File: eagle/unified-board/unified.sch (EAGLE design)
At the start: 286 parts, among them IC101 THAT151x, IC201 THAT151x, IC301 THAT151x, IC401 THAT151x, J103 phantom, J104 eqout, J105 eqout, J203 phantom, J204 eqout, J205 eqout, J303 phantom, J304 eqout, J305 eqout, J403 phantom, J404 eqout, J405 eqout, J501 out2, J601 out2, J701 power, U101 lme49710, U201 lme49710, U301 lme49710, U401 lme49710, U501 lme49710, U502 LM3915N, U601 lme49710, U602 LM3915N

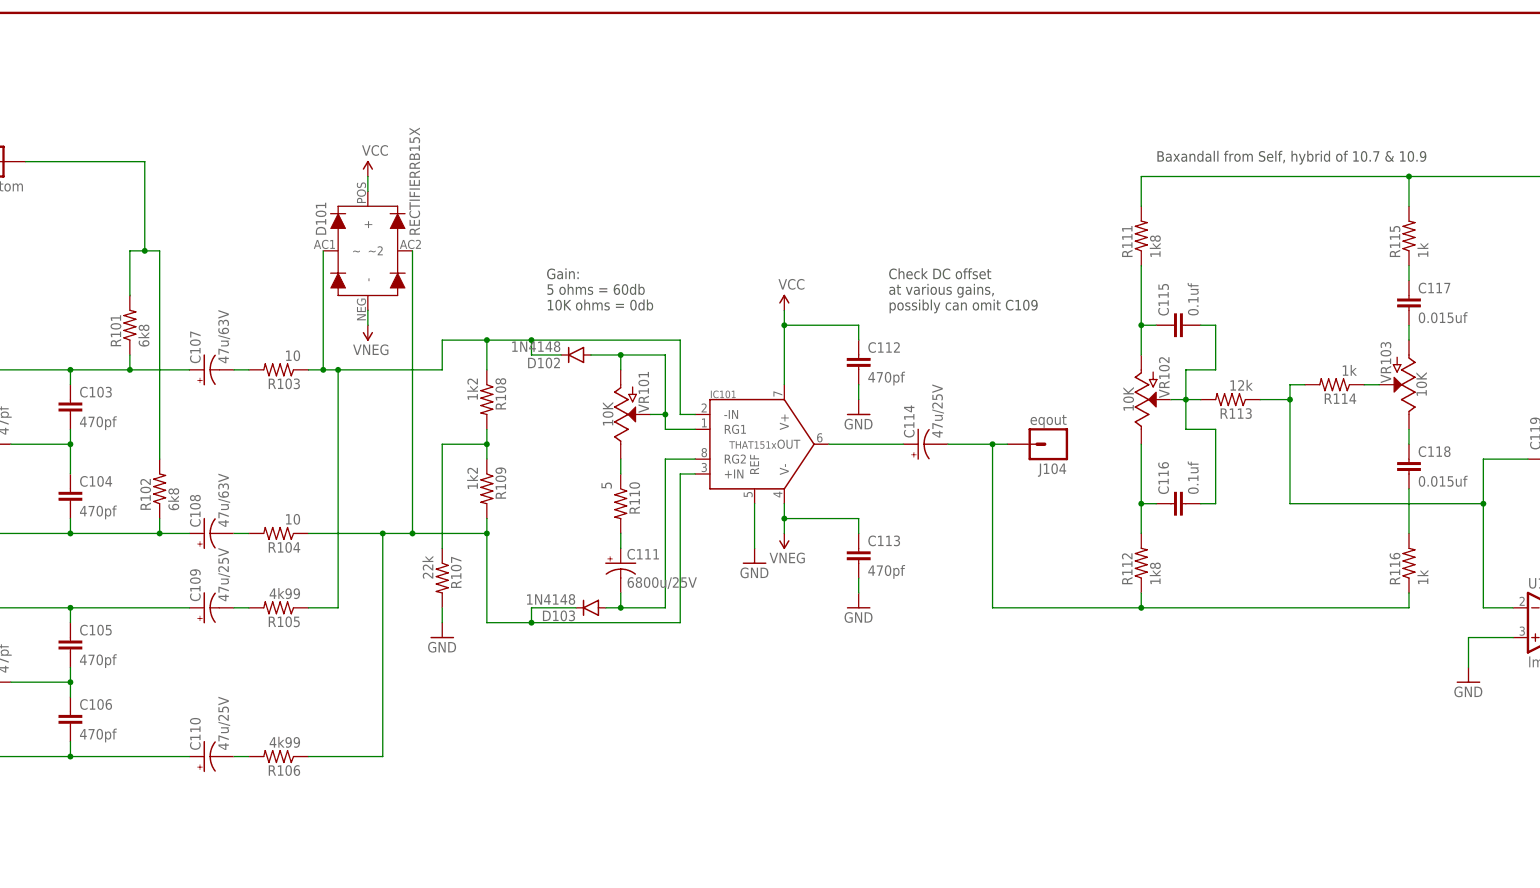
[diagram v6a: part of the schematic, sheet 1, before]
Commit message: Channels routed...
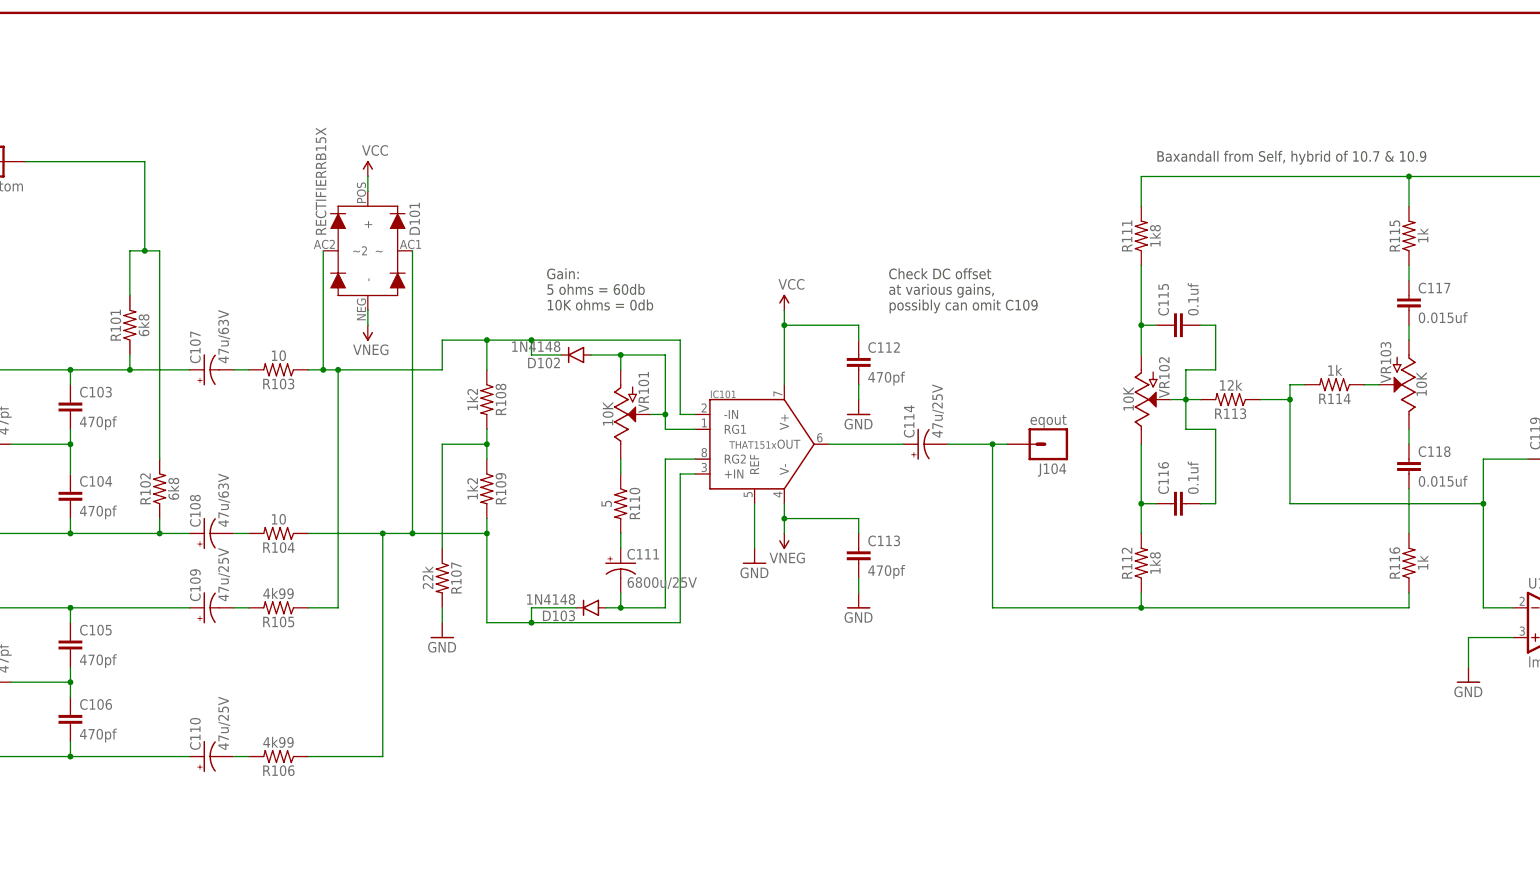
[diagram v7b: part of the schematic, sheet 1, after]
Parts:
- R101, R102, R103, R104, R105, R106, R107, R108, R109, R110, R111, R112, R113, R114, R115, R116, R201, R202, R203, R204, R205, R206, R207, R208, R209, R210, R211, R212, R213, R214, R215, R216, R301, R302, R303, R304, R305, R306, R307, R308, R309, R310, R311, R312, R313, R314, R315, R316, R401, R402, R403, R404, R405, R406, R407, R408, R409, R410, R411, R412, R413, R414, R415, R416: device SparkFun-Resistors:10KOHM-1/4W-1%(PTH)HORIZ -> mixer:RESISTOR
- R501, R502, R503, R504, R505, R506, R507, R508, R509, R510, R511, R601, R602, R603, R604, R605, R606, R607, R608, R609, R610, R611: device SparkFun-Resistors:RESISTORAXIAL-0.3 -> mixer:RESISTOR
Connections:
- net EQ1OUT1 renamed EQ2OUT
- net EQ1OUT2 renamed EQ3OUT
- net EQ1OUT3 renamed EQ4OUT
- net N$23 renamed M1GND
- net N$25 renamed M1-
- net N$26 renamed M1+
- net N$36 renamed L1GND
- net N$38 renamed L1-
- net N$39 renamed L1+
- net N$9 renamed PREOUT
- net N$114: now also D301.~2; no longer D301.~
- net N$115: now also D301.~; no longer D301.~2
- net N$146: now also D401.~2; no longer D401.~
- net N$147: now also D401.~; no longer D401.~2
- net N$30: now also D101.~2; no longer D101.~
- net N$31: now also D101.~; no longer D101.~2
- net N$82: now also D201.~2; no longer D201.~
- net N$83: now also D201.~; no longer D201.~2

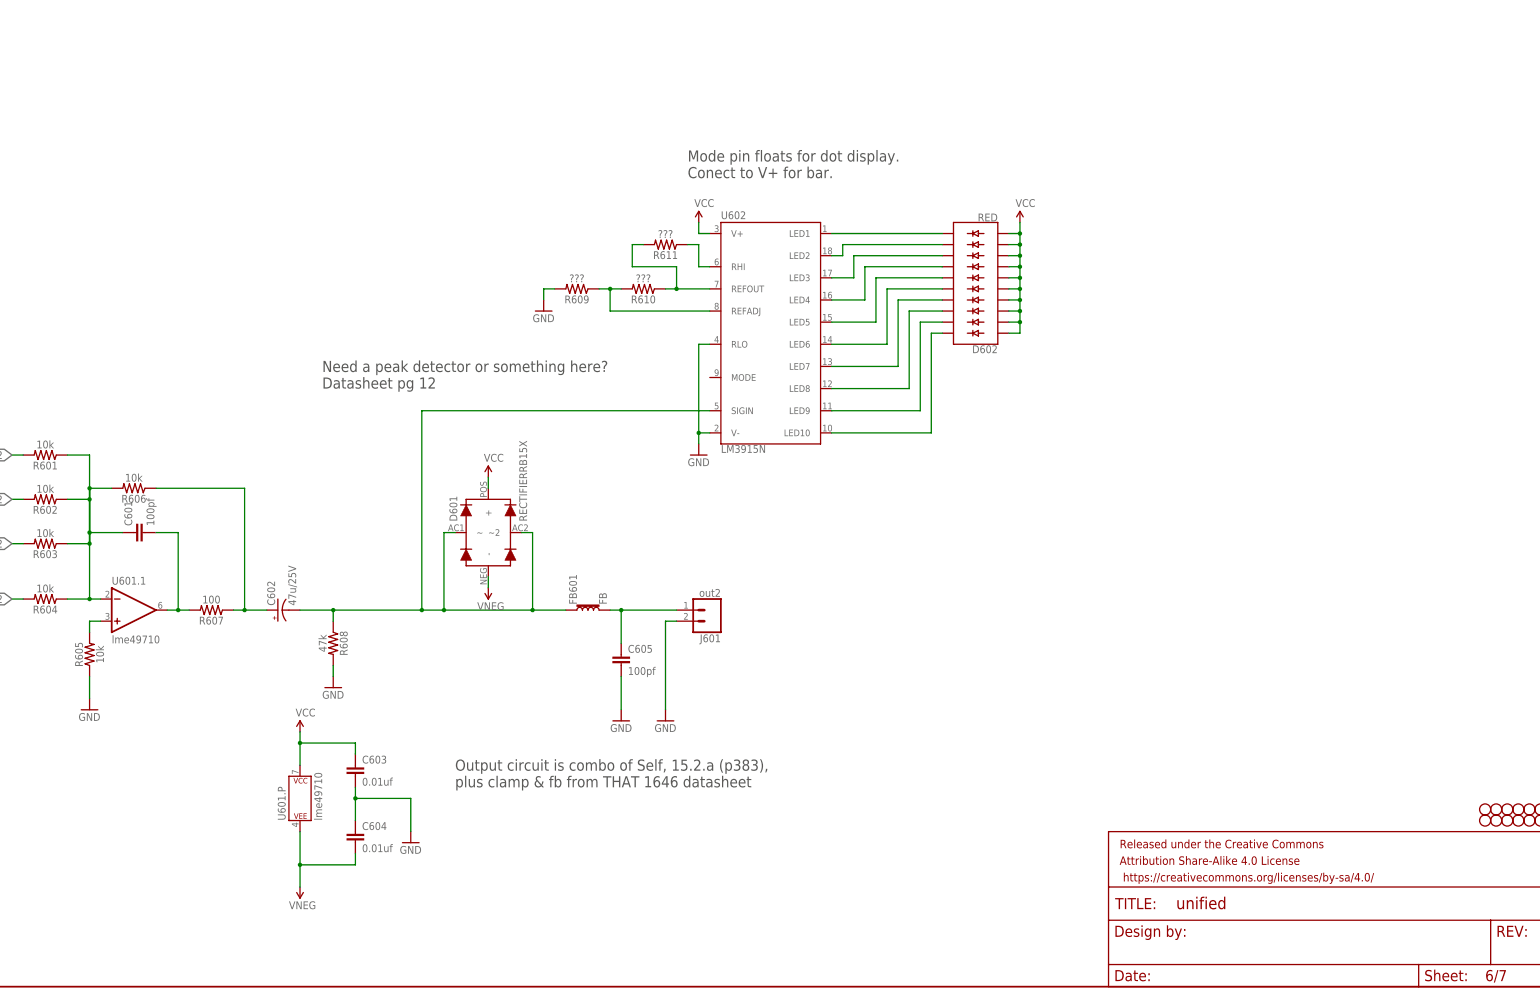
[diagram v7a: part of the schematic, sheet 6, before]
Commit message: Keeping moving.
Calculated preamp R-strings.
Tried for the bargraphs...jusy is still out...
Added peak tracker for meter circuit.
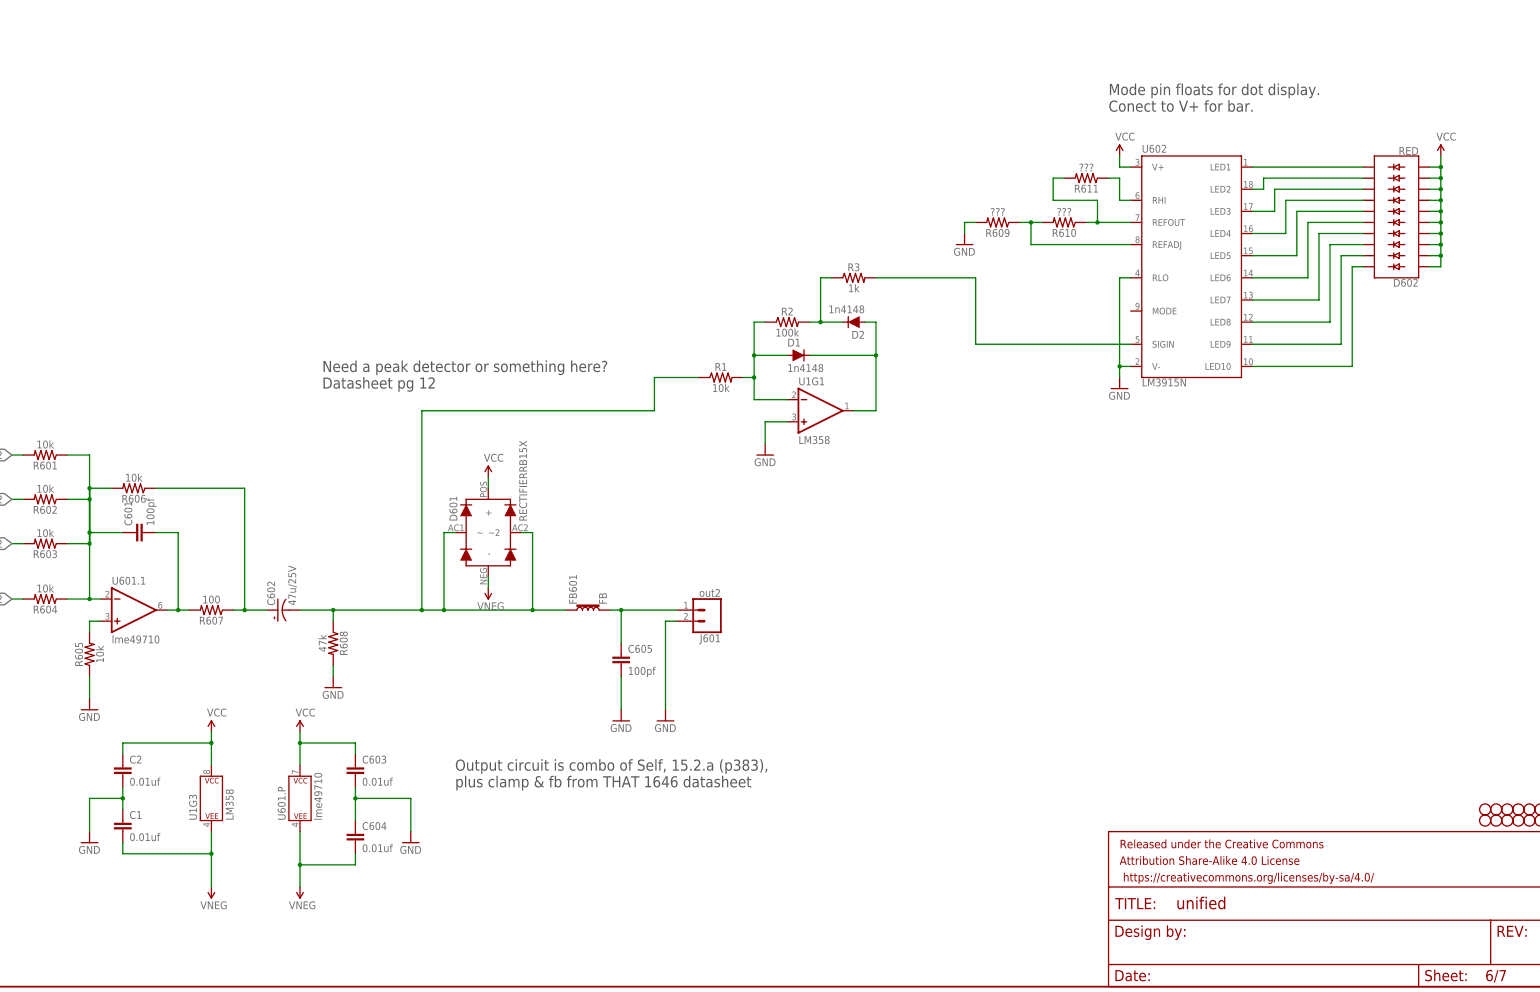
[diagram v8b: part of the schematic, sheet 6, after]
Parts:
- added C1, C2: 0.01uf, mixer:WIMA-MKS20.01UF
- added D1, D2, D3, D4: 1n4148, SparkFun-DiscreteSemi:DIODE-1N4148
- added R1, R4: 10k, mixer:RESISTOR
- added R2, R5: 100k, mixer:RESISTOR
- added R3, R6: 1k, mixer:RESISTOR
- added U1: LM358, mixer:LM358
- D102, D103, D202, D203, D302, D303, D402, D403: value 1N4148 -> 200mA/100V/1V; device SparkFun-DiscreteSemi:DIODE1N4148 -> SparkFun-DiscreteSemi:DIODE-1N4148
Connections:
- new net N$18: D2.C, R2.2, R3.1
- new net N$23: R3.2, U602.SIGIN
- new net N$25: D3.A, R4.2, R5.1, U1G2.-IN
- new net N$26: D3.C, D4.A, U1G2.OUT
- new net N$36: D4.C, R5.2, R6.1
- new net N$5: D1.A, R1.2, R2.1, U1G1.-IN
- new net N$9: D1.C, D2.A, U1G1.OUT
- net GND: now also C1.1, C2.2, U1G1.+IN, U1G2.+IN
- net N$11: now also R1.1; no longer U602.SIGIN
- net VCC: now also C2.1, U1G3.P$V+
- net VNEG: now also C1.2, U1G3.P$V-
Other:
- moved on the sheet: D602, R609, R610, R611, U602
